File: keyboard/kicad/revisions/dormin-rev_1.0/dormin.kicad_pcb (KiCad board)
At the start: 2 copper layers, 141.5 x 103.1 mm, 105 parts, among them J3 Pogo Connector, Q1 HX2302A, SW1 SW_Push, SW10 SW_Push, SW11 SW_Push, SW12 SW_Push, SW13 SW_Push, SW14 SW_Push, SW15 SW_Push, SW16 SW_Push, SW17 SW_Push, SW18 SW_Push, SW19 SW_Push, SW2 SW_Push, SW20 SW_Push, SW3 SW_Push, SW4 SW_Push, SW5 SW_Push, SW6 SW_Push, SW7 SW_Push, SW8 SW_Push, SW9 SW_Push, U3 XIAO-nRF52840-Plus-SMD, U4 TPD2E2U06DCK

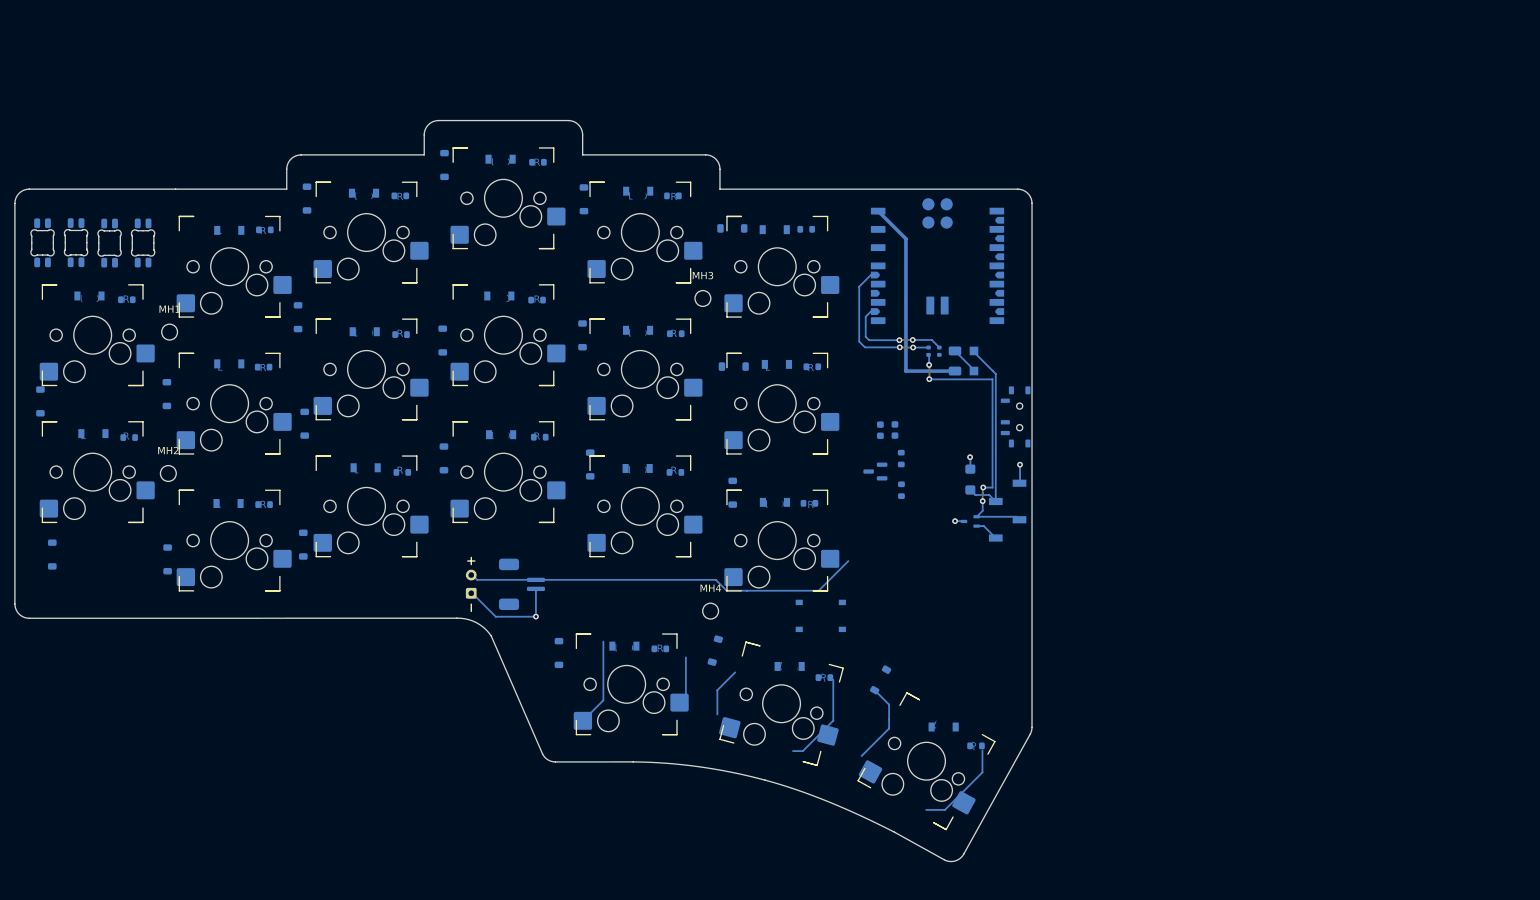
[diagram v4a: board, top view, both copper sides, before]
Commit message: feat: organize backlight components
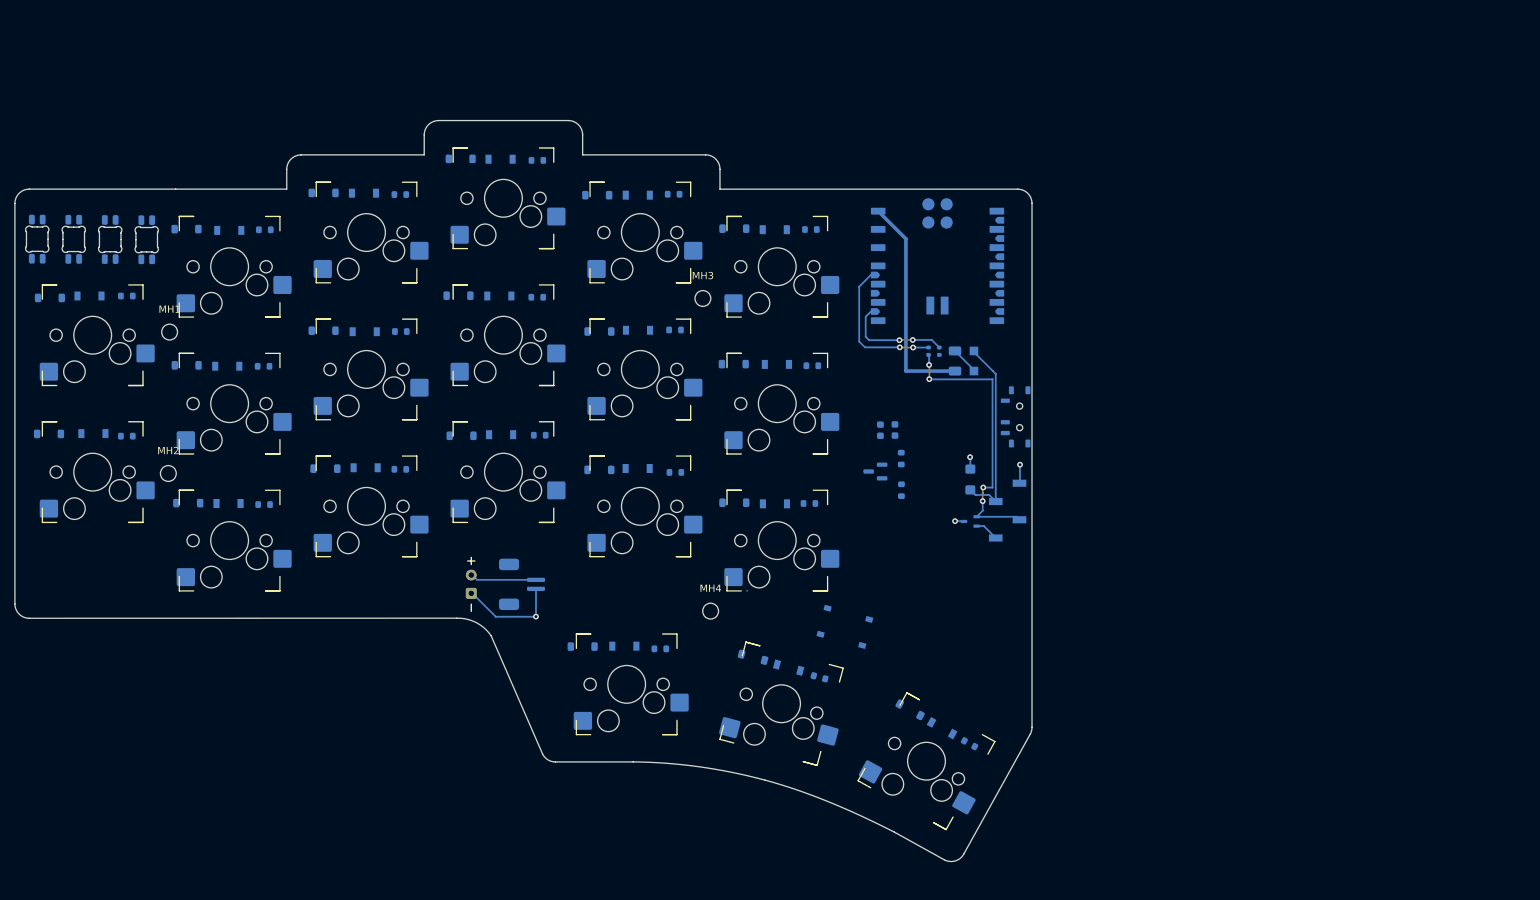
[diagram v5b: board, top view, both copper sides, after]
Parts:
- moved D5 19.8 mm to (89.5, 100.1), turned to 180 degrees
- moved D17 16.8 mm to (70.3, 128.5), turned to 180 degrees
- moved D11 14.5 mm to (70.5, 109.6), turned to 180 degrees
- moved D9 13.2 mm to (108.5, 114.2), turned to 0 degrees
- moved D15 11.0 mm to (108.8, 133.4), turned to 0 degrees
- moved D16 8.34 mm to (89.7, 138.2), turned to 0 degrees
- moved D8 6.62 mm to (127.3, 109.3), turned to 180 degrees
- moved D18 5.84 mm to (190.2, 166.9), turned to 151 degrees
- moved D19 5.34 mm to (168.3, 159.6), turned to -15 degrees
- moved D10 4.85 mm to (89.5, 119.0), turned to 180 degrees
- moved D14 3.99 mm to (127.8, 128.8), turned to 0 degrees
- moved RSW1 3.69 mm to (181.1, 155.4), turned to 165 degrees
- moved D20 3.42 mm to (144.6, 158.1), turned to 0 degrees
- moved D4 2.43 mm to (108.5, 95.0), turned to 180 degrees
- moved D7 2.41 mm to (146.9, 114.3), turned to 0 degrees
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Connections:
- R5 pad 1: EXTC -> EXTA
- R6 pad 1: EXTE -> EXTB
- U3 pad 18: EXTB -> unconnected-(U3-D14_NFC1-Pad18)
- U3 pad 19: LED_PWM -> unconnected-(U3-D15_NFC2-Pad19)
- U3 pad 20: EXTF -> LED_PWM
- U3 pad 21: EXTE -> unconnected-(U3-D17_SCK-Pad21)
- U3 pad 22: EXTD -> unconnected-(U3-D18_MISO-Pad22)
- U3 pad 23: EXTC -> EXTB
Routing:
- net Net-(BT1-+): track 55.1 -> 9.35 mm
- net Net-(D18-A): track 24.6 -> 0.00 mm
- net EXTC: track 20.5 -> 0.00 mm, vias 2 -> 0
- net (no net): track 0.00 -> 20.5 mm
- net Net-(D19-A): track 19.9 -> 0.00 mm
- net EXTE: track 15.3 -> 0.00 mm, vias 2 -> 0
- net EXTB: track 0.00 -> 15.3 mm, vias 0 -> 4
- net COL3: track 12.2 -> 0.00 mm
- net Net-(D20-A): track 6.66 -> 1.25 mm

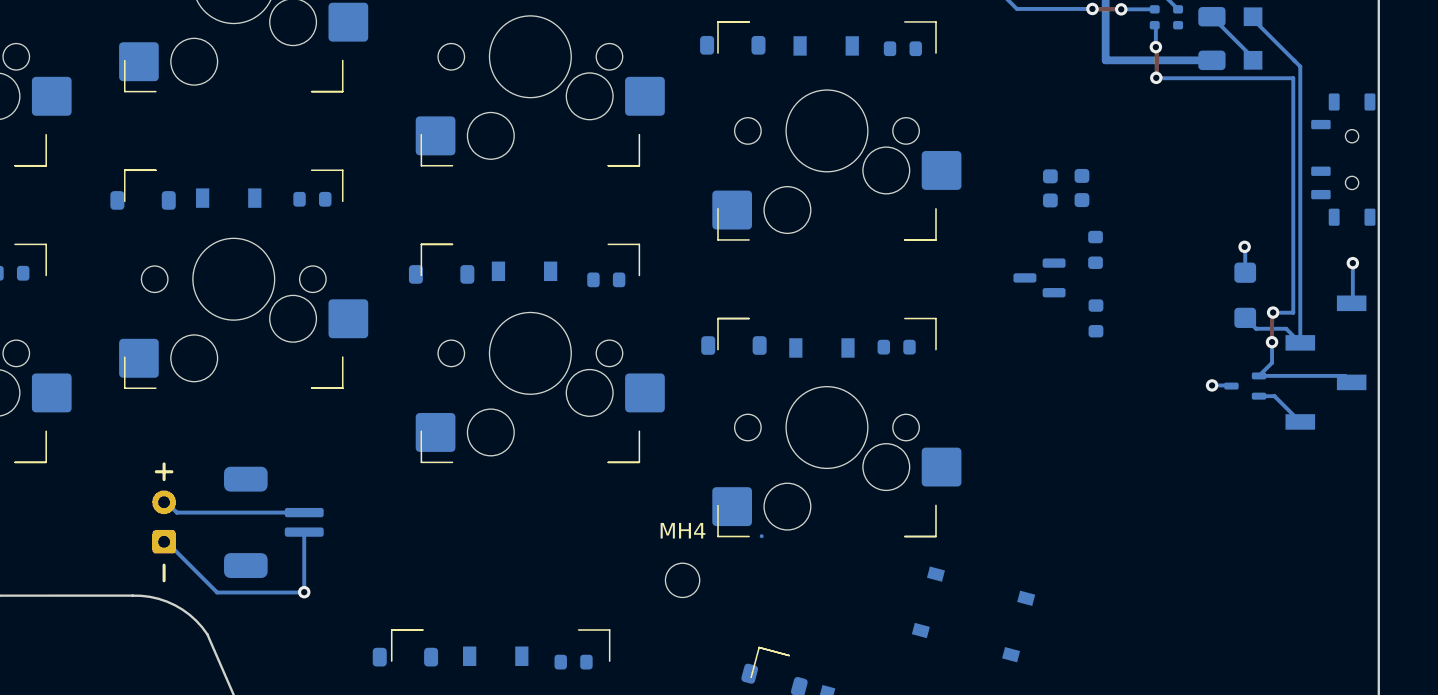
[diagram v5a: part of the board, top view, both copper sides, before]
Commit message: feat: added 3dmodels and improve components placement
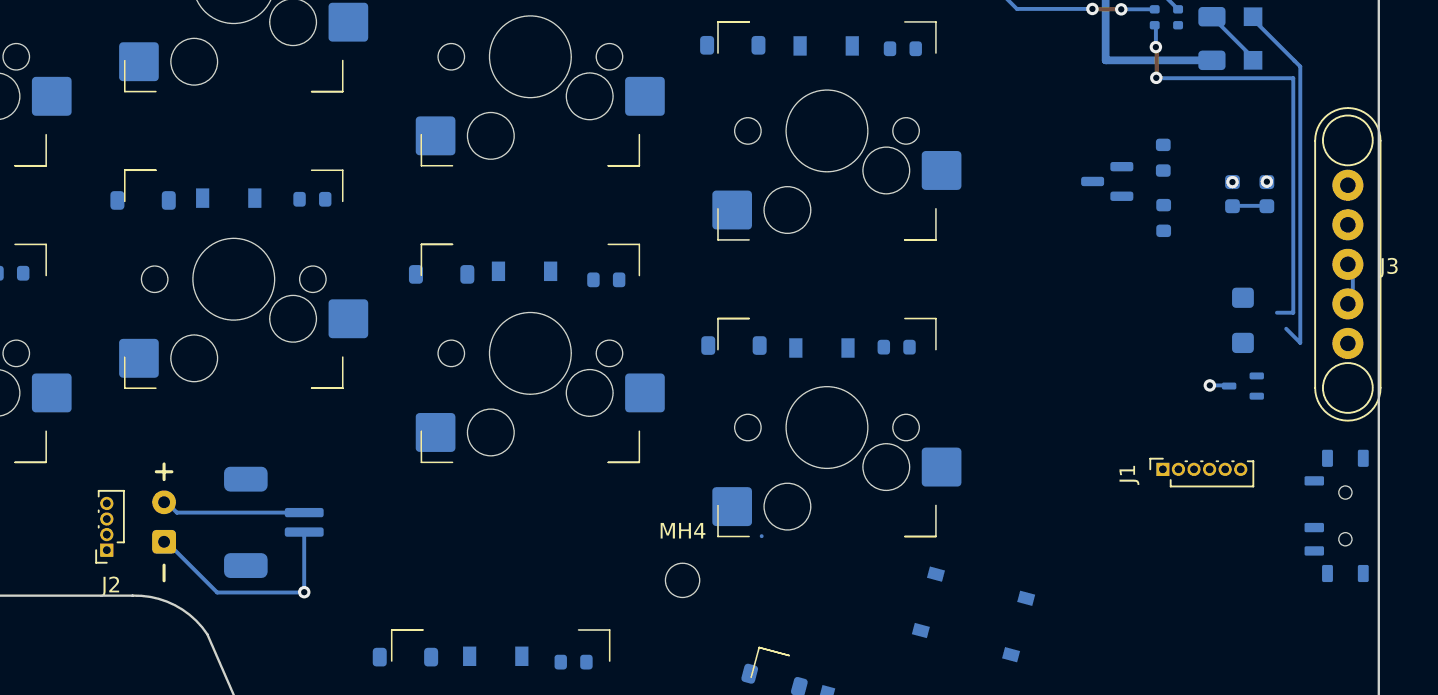
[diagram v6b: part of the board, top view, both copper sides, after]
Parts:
- added J1: Conn_01x06, Connector_PinSocket_1.00mm:PinSocket_1x06_P1.00mm_Vertical, F.Cu at (193.2, 146.1)
- added J2: Conn_01x04, Connector_PinSocket_1.00mm:PinSocket_1x04_P1.00mm_Vertical, F.Cu at (125.4, 151.3)
- C1: value 100nF -> 10uF
- C2: value 10uF -> 100nF
- J3: footprint Connector_PinSocket_2.54mm:PinSocket_1x04_P2.54mm_Vertical_SMD_Pin1Left -> willkeebs_components:MAGNET_CONN_5x2_54mm_THT; moved to F.Cu
- moved PSW1 22.9 mm to (205.0, 149.1)
- moved C2 11.9 mm to (199.9, 128.4)
- moved C1 11.7 mm to (197.7, 128.4)
- moved R707 7.78 mm to (193.3, 129.9)
- moved Q1 7.57 mm to (189.7, 127.6)
- moved R706 7.35 mm to (193.3, 126.1)
- moved J3 6.47 mm to (205.1, 132.9), turned to 0 degrees
- moved D28 1.62 mm to (198.4, 136.5)
- moved U4 0.14 mm to (198.4, 140.7)
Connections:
- RSW1 pad 1: GND -> RESET
- RSW1 pad 2: RESET -> GND
- U3 pad 21: unconnected-(U3-D17_SCK-Pad21) -> EXTD
- U3 pad 22: unconnected-(U3-D18_MISO-Pad22) -> EXTC
- U3 pad 24: Net-(U3-SWDIO) -> SWD
- U3 pad 25: Net-(U3-SWDCLK) -> SWC
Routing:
- net Net-(J3-Pin_3): track 39.2 -> 28.4 mm, vias 4 -> 2
- net Net-(J3-Pin_4): track 3.34 -> 0.00 mm
- net Net-(D27-K): track 26.4 -> 23.5 mm
- net BAT+: track 0.00 -> 2.22 mm
- net GND: track 19.8 -> 18.1 mm

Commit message: feat: updated schematics
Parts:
- removed J3: Pogo Connector, willkeebs_components:MAGNET_CONN_5x2_54mm_THT
- added J4: Conn_01x04, Connector_PinSocket_2.54mm:PinSocket_1x04_P2.54mm_Vertical, F.Cu at (204.9, 129.1)
- BT1: moved to B.Cu
- J1: footprint Connector_PinSocket_1.00mm:PinSocket_1x06_P1.00mm_Vertical -> Connector_PinSocket_2.54mm:PinSocket_1x06_P2.54mm_Vertical
- J2: footprint Connector_PinSocket_1.00mm:PinSocket_1x04_P1.00mm_Vertical -> Connector_PinSocket_2.54mm:PinSocket_1x04_P2.54mm_Vertical
- RSW1: value SW_Push -> RSW1
- moved JST1 67.2 mm to (202.1, 158.7)
- moved BT1 66.0 mm to (194.5, 158.7)
- moved J2 64.5 mm to (189.9, 148.3), turned to 90 degrees
- moved C2 11.4 mm to (196.2, 117.7)
- moved C1 11.3 mm to (194.4, 117.7)
- moved F2 10.2 mm to (186.2, 118.5), turned to -90 degrees
- moved D27 9.79 mm to (189.2, 118.5)
- moved R5 9.63 mm to (202.3, 117.1)
- moved R6 6.78 mm to (201.0, 117.1)
- moved J1 5.91 mm to (187.5, 144.8)
- moved D28 5.33 mm to (200.7, 131.7)
- moved U4 5.13 mm to (200.5, 136.0)
- moved R706 2.52 mm to (195.2, 124.4), turned to -90 degrees
- moved R707 2.41 mm to (195.2, 128.4), turned to -90 degrees
- moved Q1 2.37 mm to (191.6, 126.3)
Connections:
- net BAT+ renamed VBAT
- net Net-(BT1-+) renamed VBAT_RAW
- J1 pad 1: EXTC -> EXTA
- J1 pad 6: EXTD -> EXTB
- R5 pad 1: EXTA -> TX
- R6 pad 1: EXTB -> RX
- U3 pad 15: COL5 -> COL0
- U3 pad 16: EXTA -> COL1
- U3 pad 21: EXTD -> EXTB
- U3 pad 22: EXTC -> EXTA
- U3 pad 23: EXTB -> COL5
- U3 pad 7: COL0 -> TX
- U3 pad 8: COL1 -> RX
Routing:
- net 5V: track 30.7 -> 0.00 mm
- net Net-(J4-Pin_3): track 28.4 -> 0.00 mm, vias 2 -> 0
- net Net-(D27-K): track 23.5 -> 0.00 mm
- net (no net): track 20.5 -> 0.00 mm
- net GND: track 18.1 -> 0.00 mm, vias 4 -> 2
- net EXTB: track 15.3 -> 0.00 mm, vias 4 -> 0
- net VBAT_RAW: track 9.35 -> 0.00 mm
- net Net-(D27-A): track 3.89 -> 0.00 mm
- net VBAT: track 2.22 -> 0.00 mm
- net Net-(D1-A): track 1.25 -> 0.00 mm
- net Net-(D20-A): track 1.25 -> 0.00 mm

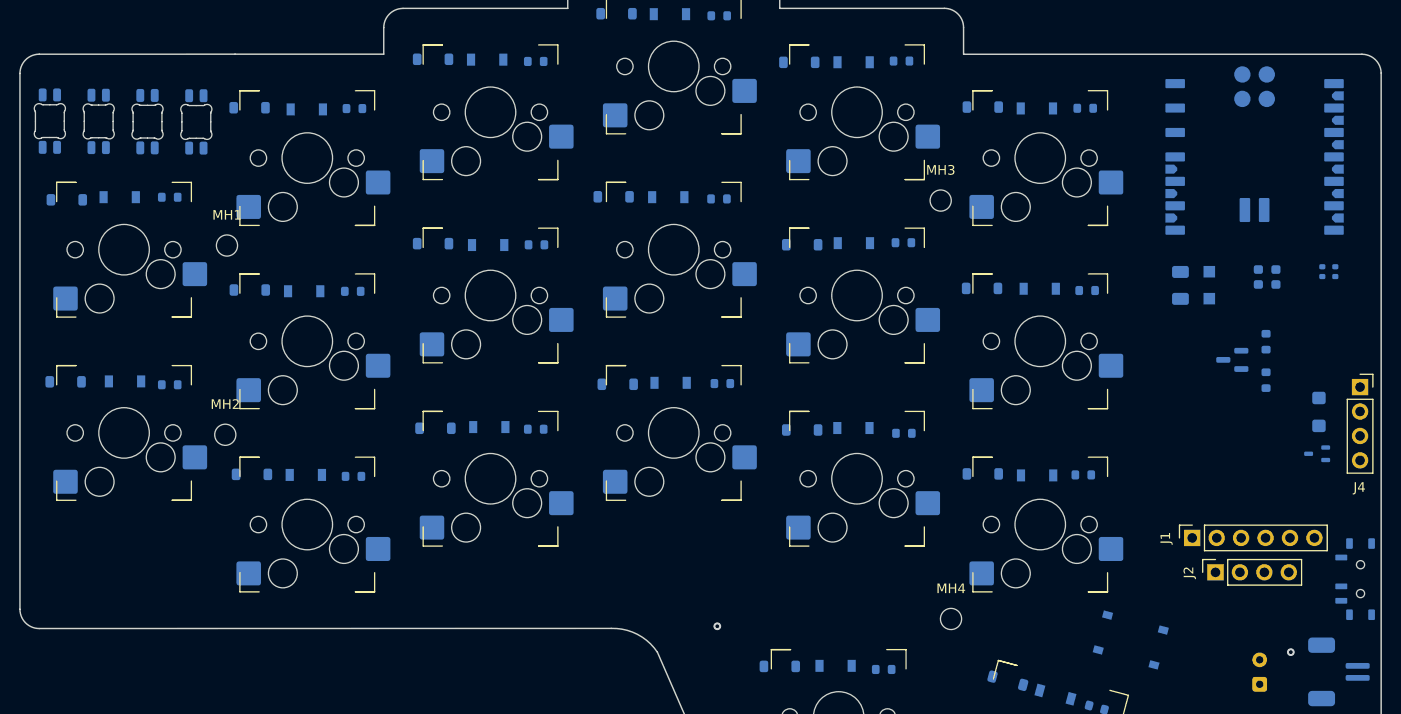
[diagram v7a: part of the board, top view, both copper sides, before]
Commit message: feat: organize pcb components placements
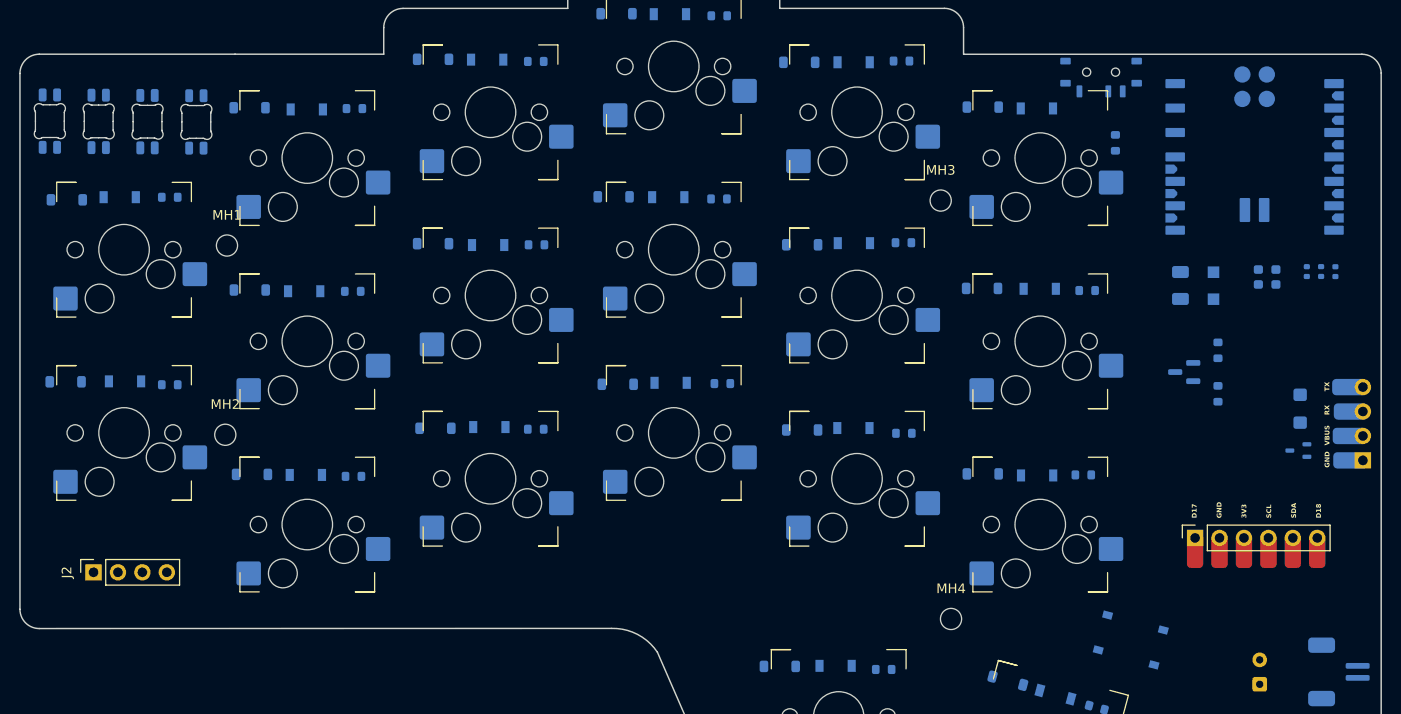
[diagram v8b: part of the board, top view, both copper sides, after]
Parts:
- removed J4: Conn_01x04, Connector_PinSocket_2.54mm:PinSocket_1x04_P2.54mm_Vertical
- added J3: Conn_01x05, willkeebs_misc:SMD_Conn_1x04_P2.54mm_Vertical, B.Cu at (205.2, 136.7)
- added R23: 100R, Resistor_SMD:R_0402_1005Metric, B.Cu at (202.4, 117.1)
- J1: footprint Connector_PinSocket_2.54mm:PinSocket_1x06_P2.54mm_Vertical -> willkeebs_misc:SMD_Conn_1x06_P2.54mm_Vertical
- moved J2 116.6 mm to (73.2, 148.3)
- moved PSW1 59.2 mm to (178.0, 96.3), turned to 180 degrees
- moved R707 5.20 mm to (190.2, 129.8)
- moved Q1 5.16 mm to (186.6, 127.5)
- moved R706 5.08 mm to (190.2, 125.3)
- moved R1 4.77 mm to (179.5, 103.7), turned to -90 degrees
- moved D28 1.98 mm to (198.7, 131.3)
- moved U4 1.98 mm to (198.5, 135.7)
- moved R6 1.61 mm to (199.4, 117.1)
- moved R5 1.48 mm to (200.9, 117.1)
- moved D27 0.44 mm to (189.7, 118.6)
- moved J1 0.30 mm to (187.8, 144.8)
- turned C1 to -90 degrees
- turned C2 to -90 degrees
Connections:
- J1 pad 4: SDA -> SCL
- J1 pad 5: SCL -> SDA
- J2 pad 3: SWD -> SWC
- J2 pad 4: SWC -> SWD
- U3 pad 18: unconnected-(U3-D14_NFC1-Pad18) -> DETECT
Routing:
- net GND: vias 2 -> 0
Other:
- board text added: "3V3"
- board text added: "D17"
- board text added: "D18"
- board text added: "GND"
- board text added: "RX"
- board text added: "SCL"
- board text added: "SDA"
- board text added: "SWCRK"
- board text added: "SWD"
- board text added: "TX"
- board text added: "VBUS"
